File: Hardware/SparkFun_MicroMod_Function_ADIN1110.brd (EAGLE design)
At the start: 38 x 65 mm, 88 parts, among them J11 MICROMOD_STANDARD, Q1 220mA/50V/3.5Ω, Q5 20V/4.2A/52mΩ/1.4W, U1 EEPROM, U2 ADIN1110, U4 3.3V, Y1 25MHz

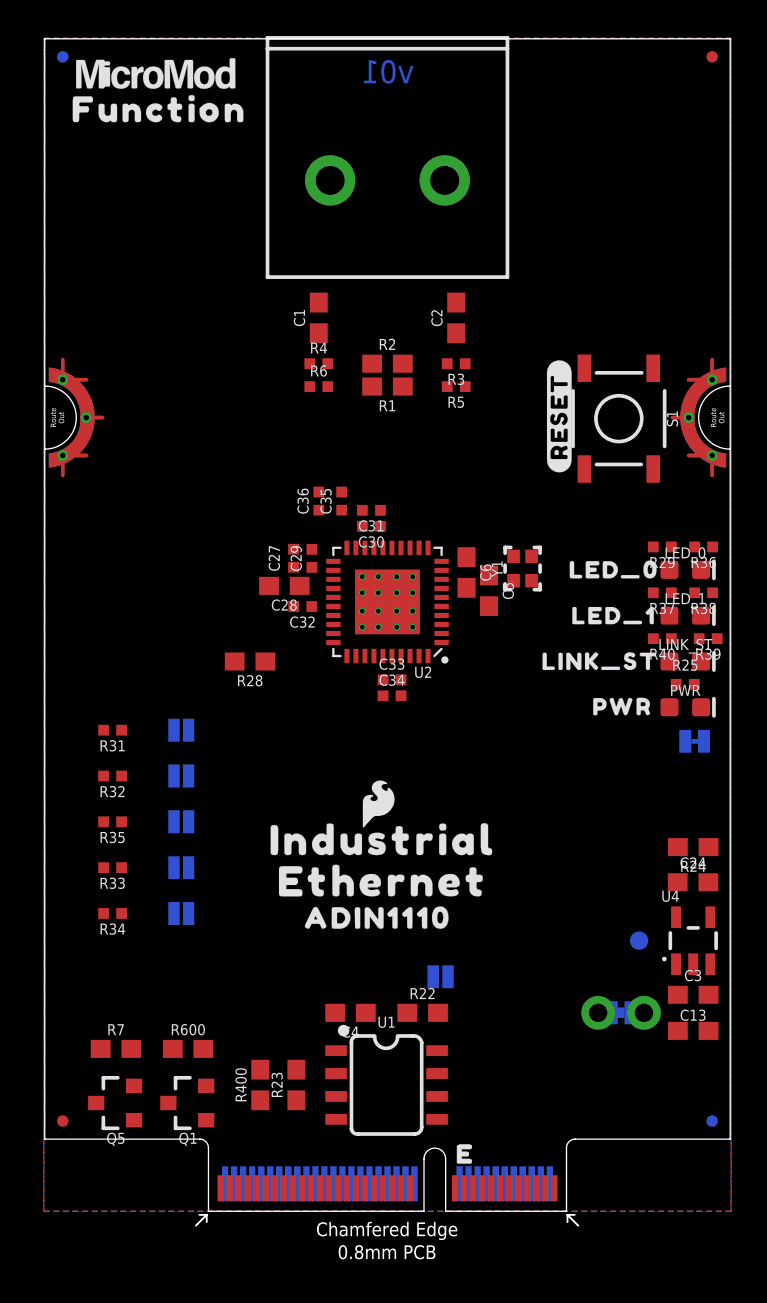
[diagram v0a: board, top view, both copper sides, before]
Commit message: HARTING T1 connector added and layout work
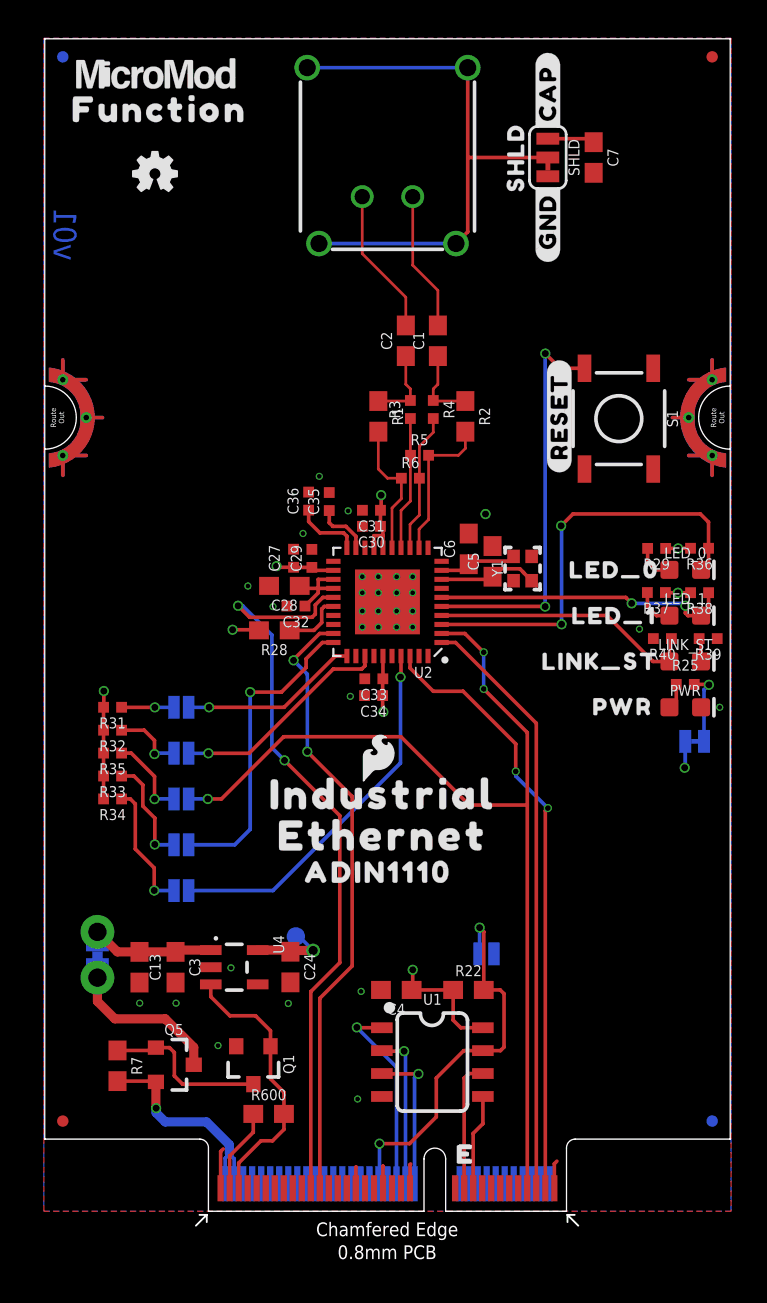
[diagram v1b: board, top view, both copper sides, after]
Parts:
- removed J2: (no value), SparkFun-Connectors:1X02_6.35_SCREWTERM
- removed R23, R24, R400: 10k, SparkFun-Resistors:0603
- added C7: 3.3nF, SparkFun-Capacitors:0603
- added J1: T1_INDUSTRIAL, ADIN1110:T1_INDUSTRIAL_JACK_AH_IP20
- added SHLD: (no value), SparkFun-Jumpers:SMT-JUMPER_3_1-NC_TRACE_SILK
- added U$10: (no value), output:#GND#13
- added U$8: (no value), output:SHLD11
- added U$9: (no value), output:#CAP#12
- J11: value MICROMOD_STANDARD -> MICROMOD_FUNCTION_STANDARD; device SparkFun-MicroMod-Function:M.2-CARD-E-22_FUNCTION_STANDARD -> SparkFun-MicroMod:M.2-CARD-E-22_FUNCTION_STANDARD
- moved LOGO3 49.6 mm to (6.16, 57.5), flipped to the top
- moved C13 30.9 mm to (5.30, 13.5), turned to 270 degrees
- moved U$28 29.6 mm to (1.21, 17.0), turned to 270 degrees
- moved MEAS 29.2 mm to (2.97, 14.2), turned to 90 degrees
- moved C3 28.7 mm to (7.30, 13.5), turned to 270 degrees
- moved U4 25.5 mm to (10.6, 13.5), turned to 270 degrees
- moved C24 22.8 mm to (13.7, 13.5), turned to 270 degrees
- moved TP1 19.0 mm to (14.0, 15.2)
- moved R6 7.18 mm to (20.3, 40.6)
- moved R4 6.84 mm to (21.6, 44.5), turned to 270 degrees
- moved C1 6.73 mm to (21.8, 48.3)
- moved R34 6.35 mm to (3.81, 22.9)
- moved R600 5.73 mm to (12.5, 5.40)
- moved R2 5.21 mm to (23.4, 44.1), turned to 270 degrees
- moved R33 5.08 mm to (3.81, 24.1)
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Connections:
- removed net ETH_!CS!: J11.49, R23.1
- removed net ETH_!INT!: J11.47, R400.1
- removed net ETH_!RST!: J11.51, R24.1
- new net N$41: C7.1, SHLD.1
- new net N$43: J1.S1, J1.S2, J1.S3, J1.S4, SHLD.2
- net !CS!: now also J11.53
- net !INT!: now also J11.55
- net 3.3V: no longer R23.2, R24.2, R400.2
- net GND: now also C7.2, SHLD.3
- net N$32: now also J1.2; no longer J2.P2
- net N$34: now also J1.1; no longer J2.P1
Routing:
- net SPI_CIPO/SPI_CFG0: track 0.00 -> 55.3 mm, vias 0 -> 3
- net !INT!: track 0.00 -> 41.7 mm, vias 0 -> 2
- net !CS!: track 0.00 -> 34.2 mm, vias 0 -> 2
- net 3.3V: track 0.00 -> 33.8 mm, vias 0 -> 10
- net SPI_SCK: track 0.00 -> 33.7 mm, vias 0 -> 2
- net SPI_COPI: track 0.00 -> 32.9 mm
- net N$43: track 0.00 -> 31.0 mm
- net LED_0: track 0.00 -> 23.6 mm, vias 0 -> 2
- net !RESET!: track 0.00 -> 22.3 mm, vias 0 -> 2
- net EWP: track 0.00 -> 21.8 mm, vias 0 -> 2
- net SPI_CFG1: track 0.00 -> 20.6 mm, vias 0 -> 1
- net !MS_SEL!: track 0.00 -> 17.4 mm, vias 0 -> 1
- net LED_1: track 0.00 -> 16.5 mm, vias 0 -> 2
- net PWR_EN: track 0.00 -> 15.2 mm
- net LINK_ST: track 0.00 -> 15.0 mm
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- added copper zone on layer 2, net 3.3V
- added copper zone on layer 15, net GND

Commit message: sch cleanup
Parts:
- removed LOGO4: SFE_LOGO_NAME_FLAME.1_INCH, SparkFun-Aesthetics:SFE_LOGO_NAME_FLAME_.1
- removed U$10: (no value), output:#GND#13
- removed U$13: (no value), output:LED_10
- removed U$9: (no value), output:#CAP#12
- added LOGO1: SFE_LOGO_NAME_FLAME.2_INCH, SparkFun-Aesthetics:SFE_LOGO_NAME_FLAME_.2
- added U$14: (no value), output:#SPI_CFG1#0
- added U$15: (no value), output:#MS_SEL#2
- added U$16: (no value), output:#SPI_CFG0#0
- added U$17: (no value), output:#SWPD_EN#1
- added U$18: (no value), output:#TX2P4_EN#2
- added U$19: (no value), output:INDUSTRIAL0
- added U$20: (no value), output:ETHERNET0
- added U$21: (no value), output:ADIN11100
- added U$23: (no value), output:LED_03
- added U$24: (no value), output:FUNCTION0
- added U$25: (no value), output:LED_14
- added U$27: (no value), output:LINK_ST15
- U$11: device output:LINK_ST0 -> output:#GND#16
- U$12: device output:LED_00 -> output:#CAP#17
- moved U$11 29.8 mm to (24.4, 59.6), flipped to the bottom
- moved U$12 24.1 mm to (31.5, 59.7), flipped to the bottom
- moved U$37 23.3 mm to (6.32, 63.0)
- moved U$8 3.53 mm to (27.9, 61.5), flipped to the bottom, turned to 0 degrees
- moved C7 2.84 mm to (27.9, 57.1), turned to 180 degrees
- moved SHLD 1.27 mm to (27.9, 59.7), flipped to the bottom, turned to 0 degrees
- moved U$7 0.25 mm to (32.3, 28.0)
- moved C6 0.15 mm to (23.4, 36.7)
- moved C29 0.15 mm to (14.8, 36.3)
- moved C27 0.15 mm to (13.8, 36.3)
- moved U$1 0.13 mm to (28.7, 44.1)
- moved C32 0.09 mm to (13.9, 33.5)
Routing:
- net N$41: track 2.62 -> 5.51 mm, vias 0 -> 1
- net N$43: track 31.0 -> 33.6 mm
- net !MS_SEL!: track 17.4 -> 18.0 mm
- added copper zone on layer 15, net 3.3V
- added copper zone on layer 2, net GND
- removed copper zone on layer 2, net 3.3V
- removed copper zone on layer 15, net GND

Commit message: some checklist catches - sch cleanup
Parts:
- removed C30: 0.1uF, SparkFun-Capacitors:0402-TIGHT
- removed R600: 10k, SparkFun-Resistors:0603
- removed U$6: (no value), output:#WP#0
- added C8: 1.0uF, SparkFun-Capacitors:0603
- added R8: 10k, SparkFun-Resistors:0603
- added U$9: (no value), output:#EWP#18
- C13: value 1.0uF -> 0.1uF; device SparkFun-Capacitors:0603 -> SparkFun-Capacitors:0402-TIGHT
- U1: value EEPROM -> ADIN1110; device SparkFun-IC-Memory:SO08 -> ADIN1110:LFCSP-40
- U2: value ADIN1110 -> EEPROM; device ADIN1110:LFCSP-40 -> SparkFun-IC-Memory:SO08
- moved C13 27.6 mm to (18.2, 38.0), turned to 180 degrees
- moved U1 25.6 mm to (19.1, 33.8), turned to 180 degrees
- moved U2 25.6 mm to (21.5, 8.27), turned to 270 degrees
- moved R22 13.0 mm to (12.5, 5.40)
- renumbered C24 to C9, C27 to C10, C28 to C11, C29 to C12, C31 to C14, C32 to C15, C33 to C16, C34 to C17, C35 to C18, C36 to C19, J11 to J2, JP5 to EWP, Q5 to Q2, R25 to R9, R28 to R10, R29 to R11, R31 to R12, R32 to R13, R33 to R14, R34 to R15, R35 to R16, R36 to R17, R37 to R20, R38 to R18, R39 to R21, R40 to R19, U4 to U3
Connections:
- net VCC renamed N$1
- removed net 5V: C13.1, C3.1, MEAS.2, MEAS.4, U3.1
- new net N$2: C3.1, C8.1, MEAS.2, MEAS.4, U3.1
- net !CS!: now also U1.29; no longer U2.29
- net !INT!: now also U1.25; no longer U2.25
- net !MS_SEL!: now also U1.30; no longer U2.30
- net !RESET!: now also U1.5; no longer U2.5
- net !SWPD_EN!: now also U1.33; no longer U2.33
- net !TX2P4_EN!: now also U1.31; no longer U2.31
- net 1.1V: now also U1.23, U1.24; no longer U2.23, U2.24
- net 3.3V: now also C13.1, R8.1, U1.16, U1.17, U1.22, U1.35, U2.8; no longer C30.1, R22.1, U1.8, U2.16, U2.17, U2.22, U2.35
- net 3.3V_IN: now also R22.1; no longer R600.1
- net A0: now also U2.1; no longer U1.1
- net A1: now also U2.2; no longer U1.2
- net A2: now also U2.3; no longer U1.3
- net EWP: now also R8.2, U2.7; no longer R22.2, U1.7
- net GND: now also C8.2, U1.EP, U2.4; no longer C30.2, U1.4, U2.EP
- net I2C_SCL: now also U2.6; no longer U1.6
- net I2C_SDA: now also U2.5; no longer U1.5
- net LED_0: now also U1.3; no longer U2.3
- net LED_1: now also U1.6; no longer U2.6
- net LINK_ST: now also U1.4; no longer U2.4
- net N$12: now also U1.8; no longer U2.8
- net N$14: now also U1.9; no longer U2.9
- net N$18: now also U1.26; no longer U2.26
- net N$21: now also U1.19; no longer U2.19
- net N$22: now also U1.20; no longer U2.20
- net N$35: now also U1.13; no longer U2.13
- net N$36: now also U1.14; no longer U2.14
- net N$37: now also U1.15; no longer U2.15
- net N$38: now also U1.12; no longer U2.12
- net PWR_EN: now also R22.2; no longer R600.2
- net SPI_CFG1: now also U1.37; no longer U2.37
- net SPI_CIPO/SPI_CFG0: now also U1.2; no longer U2.2
- net SPI_COPI: now also U1.1; no longer U2.1
- net SPI_SCK: now also U1.38; no longer U2.38
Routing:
- net N$2: track 0.00 -> 7.55 mm
- net 5V: track 7.55 -> 0.00 mm

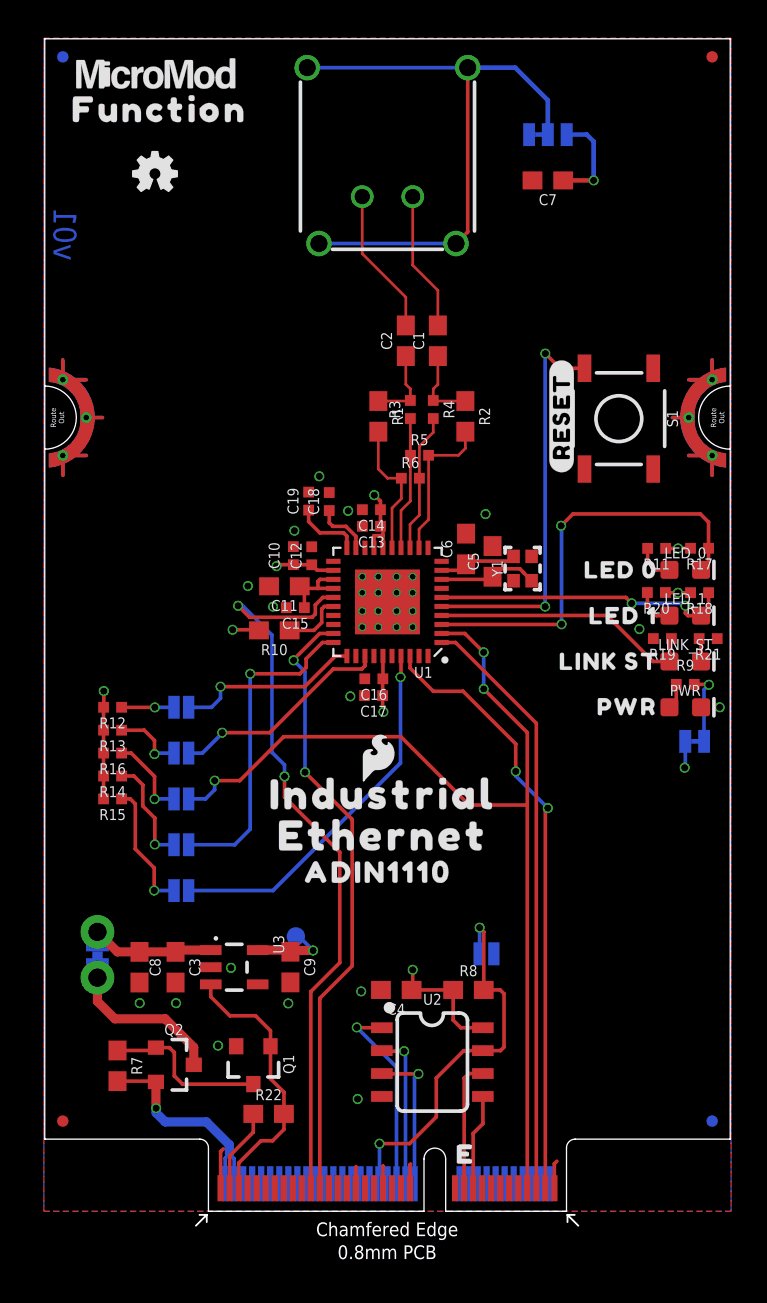
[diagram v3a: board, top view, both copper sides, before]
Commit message: Added transformer isolation and TVS diode array
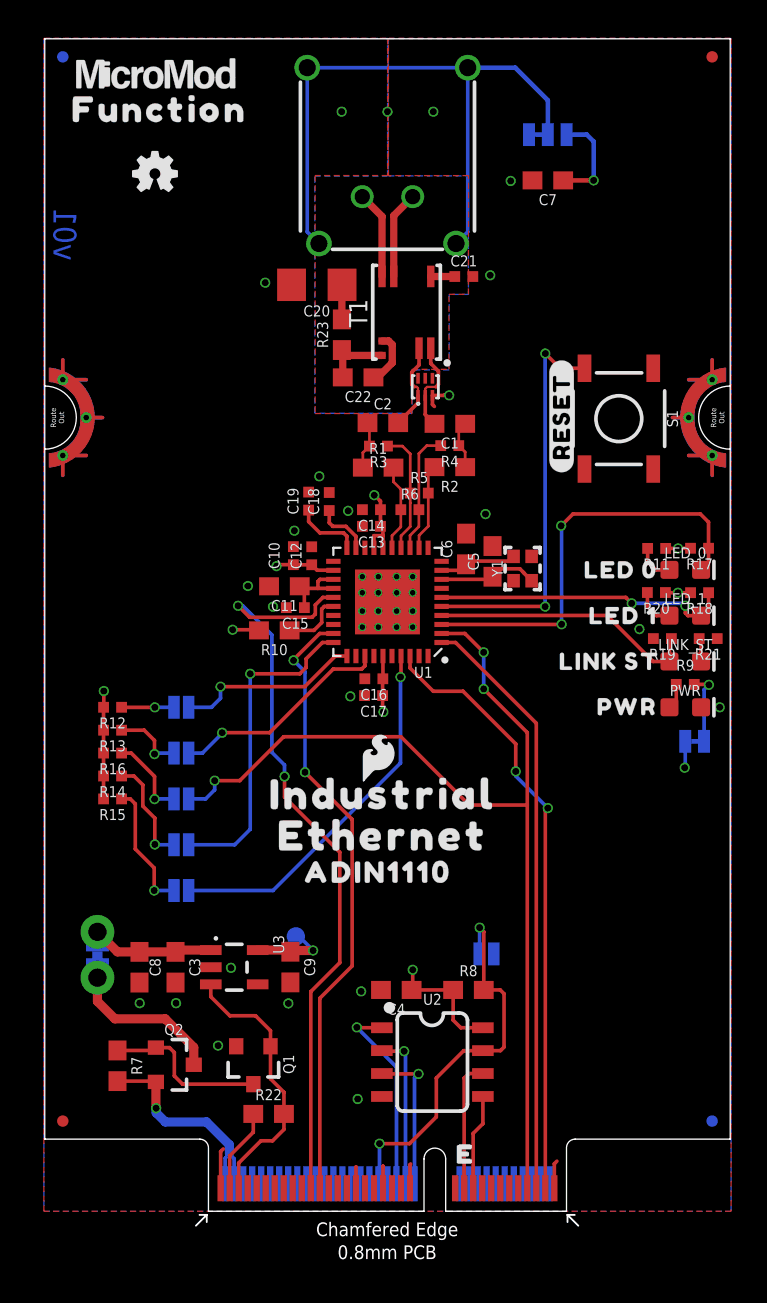
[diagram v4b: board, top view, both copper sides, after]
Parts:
- added C20: 1.0nF (2kV), SparkFun-Capacitors:1206
- added C21: 0.1uF (50V), SparkFun-Capacitors:0402-TIGHT
- added C22: 0.1uF (100V), SparkFun-Capacitors:0603
- added R23: 100, SparkFun-Resistors:0603
- added T1: WE-STST, ADIN1110:WE_STST_TRANSFORMER_1:1_SMD_3.2X4.7MM_74930030
- added U4: WE-TVS, ADIN1110:WE_TVS_1.0X1.2MM
- moved C2 4.74 mm to (18.8, 43.7), turned to 0 degrees
- moved C1 4.65 mm to (22.5, 43.7), turned to 180 degrees
- moved R2 2.94 mm to (22.5, 41.3), turned to 180 degrees
- moved R1 2.84 mm to (18.5, 41.2), turned to 0 degrees
- moved R3 2.69 mm to (18.5, 42.4), turned to 180 degrees
- moved R4 2.20 mm to (22.5, 42.4), turned to 180 degrees
- moved R5 2.10 mm to (20.8, 39.8)
- moved R6 1.75 mm to (20.3, 38.9)
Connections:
- new net N$3: C21.1, T1.5
- new net N$4: C22.1, T1.4
- new net N$5: J1.2, T1.6
- new net N$6: J1.1, T1.7
- new net N$7: C22.2, R23.1, T1.3
- new net N$8: C20.1, R23.2
- net GND: now also C20.2, C21.2, U4.3
- net N$32: now also T1.1, U4.2; no longer J1.2
- net N$34: now also T1.2, U4.1; no longer J1.1
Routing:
- net N$6: track 0.00 -> 4.88 mm
- net N$5: track 0.00 -> 4.86 mm
- net N$7: track 0.00 -> 3.88 mm
- net N$38: track 8.47 -> 4.83 mm
- net N$34: track 8.14 -> 4.99 mm
- net N$4: track 0.00 -> 3.04 mm
- net N$37: track 7.63 -> 4.82 mm
- net N$32: track 7.72 -> 5.18 mm
- net N$43: track 33.6 -> 35.9 mm
- net N$8: track 0.00 -> 1.92 mm
- net N$31: track 4.36 -> 2.67 mm
- net N$24: track 4.36 -> 2.69 mm
- net N$3: track 0.00 -> 1.34 mm
- net GND: track 8.30 -> 9.62 mm, vias 32 -> 39
- net N$35: track 7.70 -> 6.82 mm
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
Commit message: Prototype Design Review Changes
-Moved LEDs to upper edge.
-Backed off GND pour from connector for better isolation
-added jumpers to disable each LED if desired
-Schematic symbols cleanup and note corrections
-moved 3.3V testpoint to match other Ethernet MM board.
-tightened FP drills on T1 connector
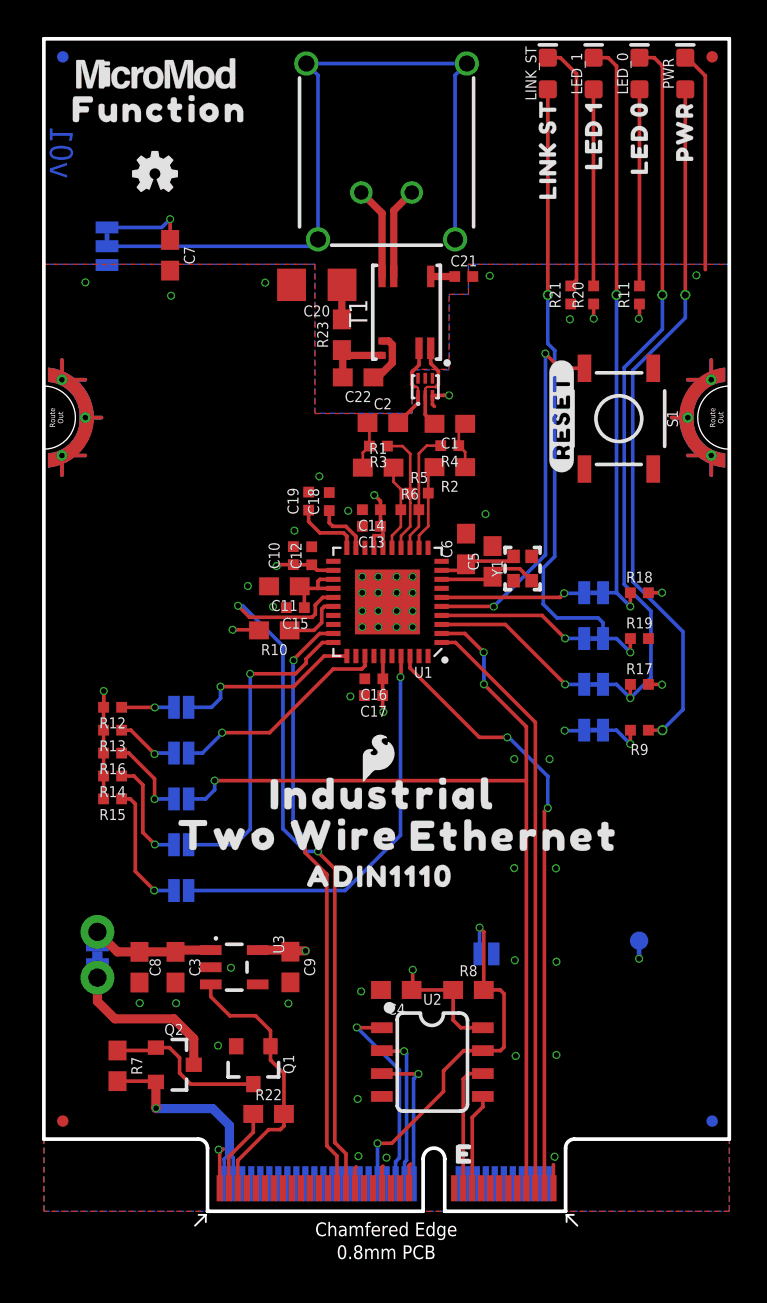
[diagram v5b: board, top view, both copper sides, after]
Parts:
- removed PWR_LED: JUMPER-SMT_2_NC_TRACE_SILK, SparkFun-Jumpers:SMT-JUMPER_2_NC_TRACE_SILK
- removed U$22: (no value), output:#PWR#0
- added LED-0, LED-1, LED-LINK, LED-PWR: JUMPER-SMT_2_NC_TRACE_SILK, SparkFun-Jumpers:SMT-JUMPER_2_NC_TRACE_SILK
- added U$10: (no value), output:#LED0#20
- added U$29: (no value), output:#LED1#21
- added U$30, U$32: (no value), output:TWO_WIRE3
- added U$31: (no value), ADIN1110:#LINKST#2
- added U$6: (no value), output:#PWR#19
- C20: value 1.0nF (2kV) -> 1.0nF/2kV
- C21: value 0.1uF (50V) -> 0.1uF/50V
- C22: value 0.1uF (100V) -> 0.1uF/100V
- R23: value 100 -> 100Ω
- R3, R4: value 5.1ohm -> 5.1Ω
- R5, R6: value 10.2ohm -> 10.2Ω
- moved PWR 35.1 mm to (35.6, 63.1), turned to 90 degrees
- moved LINK_ST 33.5 mm to (27.9, 63.1), turned to 90 degrees
- moved U$7 32.0 mm to (35.5, 59.8), turned to 90 degrees
- moved LED_1 30.5 mm to (30.5, 63.1), turned to 90 degrees
- moved U$27 28.6 mm to (27.9, 58.9), turned to 90 degrees
- moved U$12 28.1 mm to (3.55, 57.1), turned to 270 degrees
- moved LED_0 27.6 mm to (33.0, 63.1), turned to 90 degrees
- moved U$8 27.4 mm to (1.75, 53.5), turned to 270 degrees
- moved U$25 26.7 mm to (30.5, 59.6), turned to 90 degrees
- moved SHLD 25.2 mm to (3.50, 53.5), turned to 90 degrees
- moved U$23 24.0 mm to (33.0, 59.5), turned to 90 degrees
- moved U$11 23.0 mm to (3.45, 50.0), turned to 270 degrees
- moved C7 21.3 mm to (7.00, 53.0), turned to 270 degrees
- moved R21 20.5 mm to (29.2, 50.8), turned to 90 degrees
- moved TP1 19.0 mm to (33.0, 15.0)
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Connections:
- net N$5 renamed DA-
- net N$6 renamed DA+
- new net N$5: LED-LINK.1, LINK_ST.A, R19.1
- new net N$6: LED-1.1, LED_1.C, R18.1
- new net N$9: LED-0.1, LED_0.C, R17.1
- net !CS!: now also J2.49; no longer J2.53
- net !INT!: now also J2.47; no longer J2.55
- net 3.3V: now also LED-PWR.2; no longer PWR_LED.2
- net GND: now also SHLD.1; no longer SHLD.3
- net LED_0: now also LED-0.2; no longer LED_0.C, R17.1
- net LED_1: now also LED-1.2; no longer LED_1.C, R18.1
- net LINK_ST: now also LED-LINK.2; no longer LINK_ST.A, R19.1
- net N$19: now also LED-PWR.1; no longer PWR_LED.1
- net N$41: now also SHLD.3; no longer SHLD.1
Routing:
- net N$9: track 0.00 -> 41.1 mm, vias 0 -> 2
- net N$20: track 1.43 -> 39.1 mm, vias 0 -> 2
- net N$5: track 0.00 -> 36.2 mm, vias 0 -> 2
- net N$6: track 0.00 -> 33.3 mm, vias 0 -> 2
- net LED_0: track 23.6 -> 9.29 mm, vias 2 -> 1
- net N$33: track 1.31 -> 13.9 mm
- net GND: track 9.62 -> 21.7 mm, vias 39 -> 49
- net N$23: track 2.14 -> 10.9 mm
- net N$30: track 2.21 -> 10.9 mm
- net LED_1: track 16.5 -> 8.02 mm, vias 2 -> 1
- net LINK_ST: track 15.0 -> 8.44 mm, vias 0 -> 1
- net N$43: track 35.9 -> 40.8 mm
- net SPI_CIPO/SPI_CFG0: track 55.5 -> 52.9 mm
- net SPI_CFG1: track 20.6 -> 23.0 mm
- net !RESET!: track 22.3 -> 20.6 mm
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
